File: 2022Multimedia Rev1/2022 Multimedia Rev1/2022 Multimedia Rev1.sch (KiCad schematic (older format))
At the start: 19 parts, among them U1 OKI, U2 OKI, U3 BDJ2GA5WEFJ, U4 TM4C129E_Launchpad

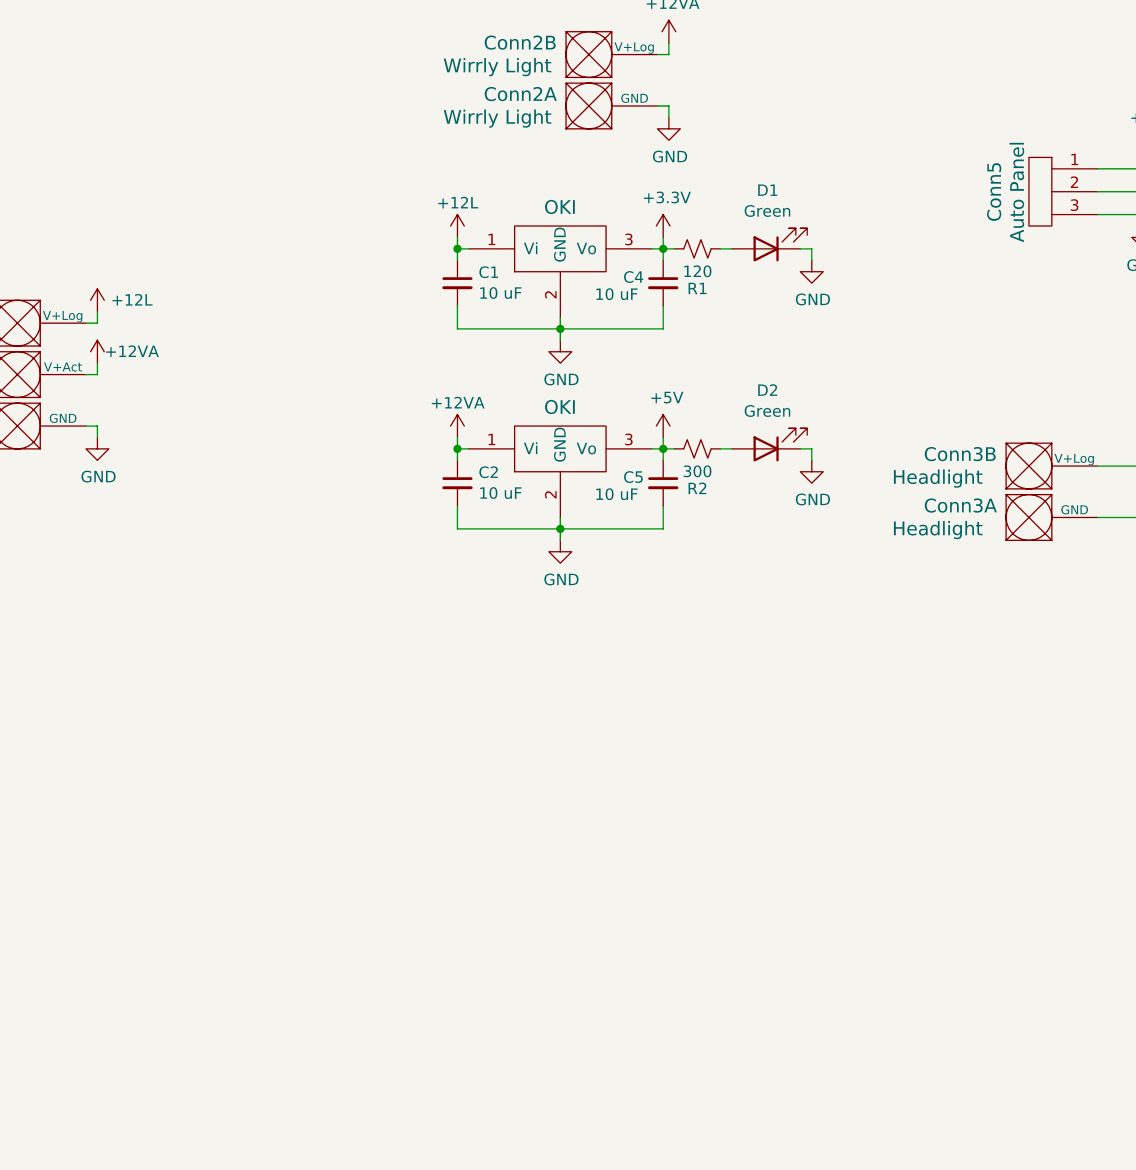
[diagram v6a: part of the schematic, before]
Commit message: change oki to china buck
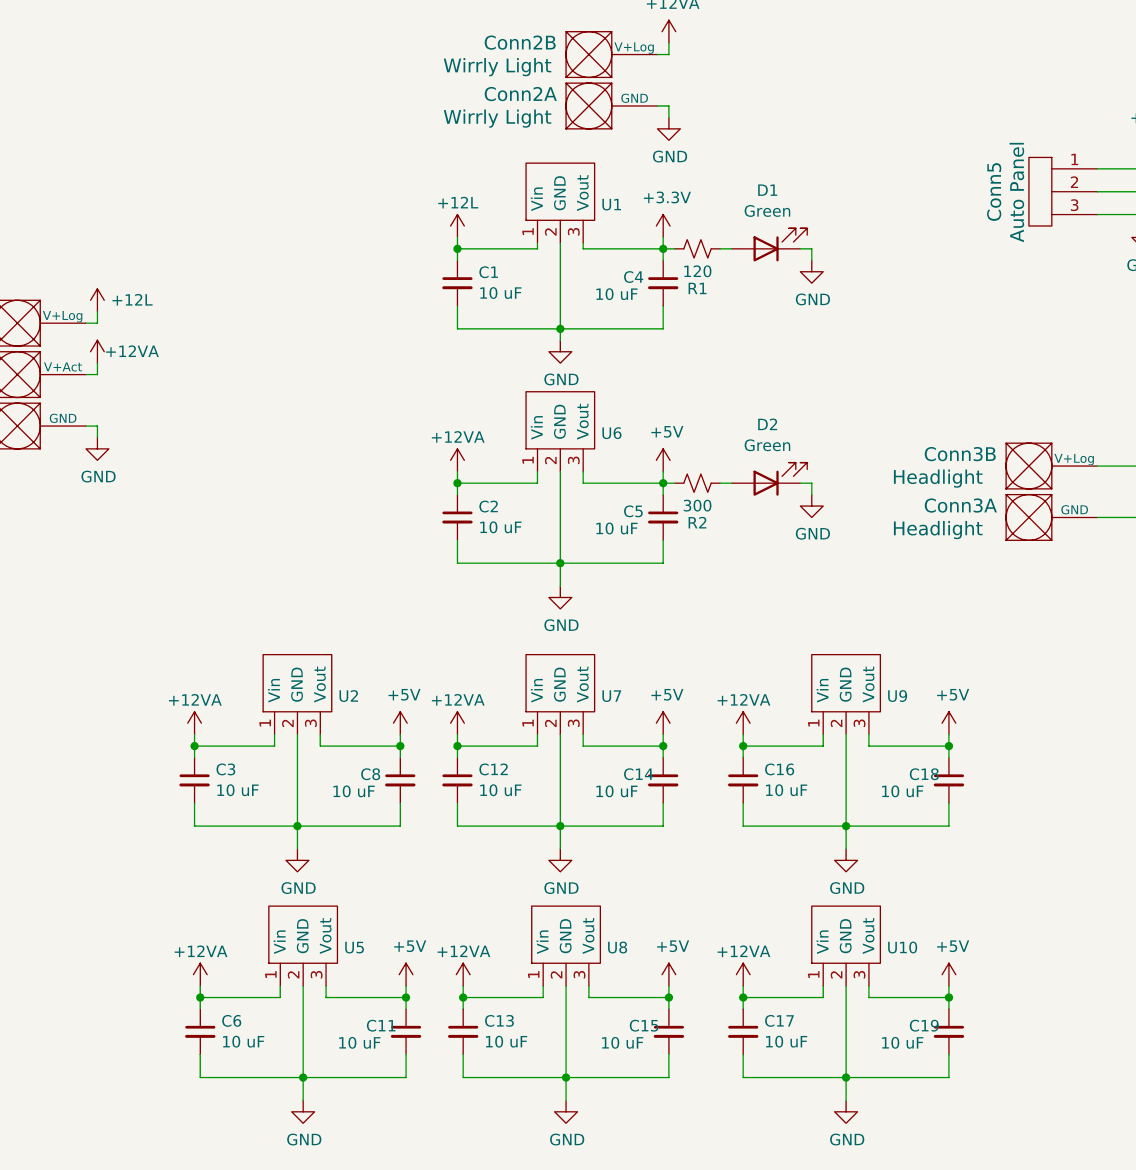
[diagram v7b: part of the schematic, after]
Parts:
- removed U1, U2: OKI, MRDT_Devices:OKI_Horizontal, symbol MRDT_Devices:OKI
- added C11, C12, C13, C14, C15, C16, C17, C18, C19, C3, C6, C8: 10 uF, Capacitor_SMD:C_0603_1608Metric_Pad1.05x0.95mm_HandSolder, symbol Device:C_Small
- added U1, U10, U2, U5, U6, U7, U8, U9: TSR1-2433, MRDT_Devices:TSR_1-2433, symbol MRDT_Devices:TSR1-2433
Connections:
- net +12L: now also U1.1 (Vin)
- net +12VA: now also C12.1, C13.1, C16.1, C17.1, C3.1, C6.1, U10.1 (Vin), U2.1 (Vin), U5.1 (Vin), U6.1 (Vin), U7.1 (Vin), U8.1 (Vin), U9.1 (Vin)
- net +3V3: now also U1.3 (Vout)
- net +5V: now also C11.1, C14.1, C15.1, C18.1, C19.1, C8.1, U10.3 (Vout), U2.3 (Vout), U5.3 (Vout), U6.3 (Vout), U7.3 (Vout), U8.3 (Vout), U9.3 (Vout)
- net GND: now also C11.2, C12.2, C13.2, C14.2, C15.2, C16.2, C17.2, C18.2, C19.2, C3.2, C6.2, C8.2, U1.2 (GND), U10.2 (GND), U2.2 (GND), U5.2 (GND), U6.2 (GND), U7.2 (GND), U8.2 (GND), U9.2 (GND)
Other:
- moved on the sheet: C2, C5, D2, R2

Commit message: Finished rev2
gerbs and all, except bom
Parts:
- removed C11, C12, C13, C14, C15, C16, C17, C18, C19, C2, C3, C5, C6, C8: 10 uF, Capacitor_SMD:C_0603_1608Metric_Pad1.05x0.95mm_HandSolder, symbol Device:C_Small
- removed Conn5: Auto Panel, MRDT_Connectors:MOLEX_uF_S_03_Horizontal, symbol MRDT_Connectors:Molex_uF_S_03
- removed U10, U2, U5, U6, U7, U8, U9: TSR1-2433, MRDT_Devices:TSR_1-2433, symbol MRDT_Devices:TSR1-2433
- added Conn4: AndersonPP, MRDT_Connectors:Square_Anderson_2_H_Side_By_Side, symbol MRDT_Connectors:AndersonPP
- added Conn5: Neopixel Power, MRDT_Connectors:MOLEX_uF_S_02_Horizontal, symbol MRDT_Connectors:Molex_uF_S_02
- added U2: China5V8ABuck, 2022 Multimedia Rev1:China5V8ABuck, symbol Multimedia_IC:China5V8ABuck
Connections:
- net +12VA: now also U2.1 (12V)
- net +5V: now also Conn4.2 (V+Log), U2.4 (5V)
- net AutopanelNeoPixel: now also Conn5.1
- net GND: now also Conn4.1 (GND), Conn5.2, U2.2 (GND), U2.3 (GND)
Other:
- moved on the sheet: C7, D2, R2
